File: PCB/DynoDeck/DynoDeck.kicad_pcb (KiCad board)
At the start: 2 copper layers, 0 parts

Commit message: Footprints
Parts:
- added BT1: Batt, Connector_JST:JST_PH_S2B-PH-K_1x02_P2.00mm_Horizontal, F.Cu at (137.2, 79.6)
- added C1: 47u, Capacitor_SMD:C_0603_1608Metric, F.Cu at (94.8, 78.4)
- added C10: 4u7, Capacitor_SMD:C_0603_1608Metric, F.Cu at (98.9, 78.4)
- added C11: 10u, Capacitor_SMD:C_0603_1608Metric, F.Cu at (98.9, 80.9)
- added C12: 10u, Capacitor_SMD:C_0603_1608Metric, F.Cu at (98.9, 83.5)
- added C13: 10u, Capacitor_SMD:C_0603_1608Metric, F.Cu at (98.9, 86.0)
- added C14: 4u7, Capacitor_SMD:C_0603_1608Metric, F.Cu at (98.9, 88.5)
- added C15: 47p, Capacitor_SMD:C_0603_1608Metric, F.Cu at (98.9, 91.0)
- added C16: 100n, Capacitor_SMD:C_0603_1608Metric, F.Cu at (98.9, 93.5)
- added C17: 47n, Capacitor_SMD:C_0603_1608Metric, F.Cu at (98.9, 96.0)
- added C18: 470n, Capacitor_SMD:C_0603_1608Metric, F.Cu at (98.9, 98.5)
- added C19: 4u7, Capacitor_SMD:C_0603_1608Metric, F.Cu at (102.9, 78.4)
- added C2: 100n, Capacitor_SMD:C_0603_1608Metric, F.Cu at (94.8, 80.9)
- added C20: 4u7, Capacitor_SMD:C_0603_1608Metric, F.Cu at (102.9, 80.9)
- added C21: 220n, Capacitor_SMD:C_0603_1608Metric, F.Cu at (102.9, 83.5)
- added C22: 100n, Capacitor_SMD:C_0603_1608Metric, F.Cu at (102.9, 86.0)
- added C24: 100n, Capacitor_SMD:C_0603_1608Metric, F.Cu at (102.9, 88.5)
- added C25: 100p, Capacitor_SMD:C_0402_1005Metric, F.Cu at (143.2, 96.0)
- added C26: 100n, Capacitor_SMD:C_0603_1608Metric, F.Cu at (102.9, 91.0)
- added C27: 10u, Capacitor_SMD:C_0603_1608Metric, F.Cu at (102.9, 93.5)
- added C3: 1u, Capacitor_SMD:C_0603_1608Metric, F.Cu at (94.8, 83.5)
- added C4: 1u, Capacitor_SMD:C_0603_1608Metric, F.Cu at (94.8, 86.0)
- added C5: 10p, Capacitor_SMD:C_0603_1608Metric, F.Cu at (94.8, 88.5)
- added C6: 100n, Capacitor_SMD:C_0603_1608Metric, F.Cu at (94.8, 91.0)
- added C7: 100n, Capacitor_SMD:C_0603_1608Metric, F.Cu at (94.8, 93.5)
- added C8: 100n, Capacitor_SMD:C_0603_1608Metric, F.Cu at (94.8, 96.0)
- added C9: 47n, Capacitor_SMD:C_0603_1608Metric, F.Cu at (94.8, 98.5)
- added D1: STAT, LED_SMD:LED_0603_1608Metric, F.Cu at (103.3, 104.7)
- added D2: D_Schottky, Diode_SMD:D_SMB, F.Cu at (129.1, 97.2)
- added FB1: 600@100Mhz, Inductor_SMD:L_0603_1608Metric_Pad1.05x0.95mm_HandSolder, F.Cu at (95.0, 104.7)
- added FL1: 0900FM15K0039, RF_Converter:Balun_Johanson_0900FM15K0039, F.Cu at (143.5, 92.8)
- added J1: USB_C_Receptacle_USB2.0_16P, Connector_USB:USB_C_Receptacle_G-Switch_GT-USB-7010ASV, F.Cu at (118.7, 92.2)
- added J2: PGRM, PGRMPins:PogoPin_1x05_P2.54mm_Pad1.8mm, F.Cu at (94.7, 101.6)
- added J3: CardKB, Connector_JST:JST_PH_S4B-PH-K_1x04_P2.00mm_Horizontal, F.Cu at (115.9, 79.6)
- added J4: E-paper, Connector_PinSocket_2.54mm:PinSocket_2x04_P2.54mm_Vertical, F.Cu at (137.7, 58.9)
- added J5: HC-IPEX0125-01 (u.FL), Connector_Coaxial:U.FL_Molex_MCRF_73412-0110_Vertical, F.Cu at (109.7, 102.9)
- added J6: BWSMA-KWE-Z001 (SMA), Connector_Coaxial:SMA_BAT_Wireless_BWSMA-KWE-Z001, F.Cu at (129.5, 89.7)
- added L1: 2u2, Inductor_SMD:L_Sunlord_MWSA0503S, F.Cu at (138.0, 90.2)
- added L2: 47n, Inductor_SMD:L_1008_2520Metric, F.Cu at (144.6, 83.7)
- added L3: 15u, Inductor_SMD:L_Sunlord_MWSA0503S, F.Cu at (138.0, 97.0)
- added R1: 10k, Resistor_SMD:R_0603_1608Metric, F.Cu at (102.9, 96.0)
- added R10: 10k, Resistor_SMD:R_0603_1608Metric, F.Cu at (106.9, 96.0)
- added R11: 5k1, Resistor_SMD:R_0603_1608Metric, F.Cu at (106.9, 98.5)
- added R12: 100k, Resistor_SMD:R_0603_1608Metric, F.Cu at (110.9, 78.4)
- added R13: 100k, Resistor_SMD:R_0603_1608Metric, F.Cu at (110.9, 80.9)
- added R14: 100k, Resistor_SMD:R_0603_1608Metric, F.Cu at (110.9, 83.5)
- added R15: 887k, Resistor_SMD:R_0603_1608Metric, F.Cu at (110.9, 86.0)
- added R16: 10k, Resistor_SMD:R_0603_1608Metric, F.Cu at (110.9, 88.5)
- added R17: 47, Resistor_SMD:R_0603_1608Metric, F.Cu at (110.9, 91.0)
- added R18: 10k, Resistor_SMD:R_0603_1608Metric, F.Cu at (110.9, 93.5)
- added R19: 100k, Resistor_SMD:R_0603_1608Metric, F.Cu at (110.9, 96.0)
- added R2: 4k7, Resistor_SMD:R_0603_1608Metric, F.Cu at (102.9, 98.5)
- added R3: 10k, Resistor_SMD:R_0603_1608Metric, F.Cu at (106.9, 78.4)
- added R4: 4k7, Resistor_SMD:R_0603_1608Metric, F.Cu at (106.9, 80.9)
- added R5: 220, Resistor_SMD:R_0603_1608Metric, F.Cu at (106.9, 83.5)
- added R6: 10k, Resistor_SMD:R_0603_1608Metric, F.Cu at (106.9, 86.0)
- added R7: 260, Resistor_SMD:R_0603_1608Metric, F.Cu at (106.9, 88.5)
- added R8: 10k, Resistor_SMD:R_0603_1608Metric, F.Cu at (106.9, 91.0)
- added R9: 10k, Resistor_SMD:R_0603_1608Metric, F.Cu at (106.9, 93.5)
- added SW1: QON, Button_Switch_SMD:SW_SPST_TS-1088-xR020, F.Cu at (143.5, 58.9)
- added SW2: POWER, Button_Switch_SMD:SW_SPDT_CK_JS102011SAQN, F.Cu at (118.4, 101.9)
- added SW3: RESET, Button_Switch_SMD:SW_SPST_TS-1088-xR020, F.Cu at (143.5, 63.4)
- added SW4: IO1, Button_Switch_SMD:SW_SPST_PTS647_Sx38, F.Cu at (129.0, 103.2)
- added U1: BQ25895RTW, Package_DFN_QFN:Texas_RTW_WQFN-24-1EP_4x4mm_P0.5mm_EP2.7x2.7mm_ThermalVias, F.Cu at (143.1, 72.0)
- added U2: USBLC6-2SC6, Package_TO_SOT_SMD:SOT-23-6, F.Cu at (144.7, 79.6)
- added U3: SX1262IMLTRT, Package_DFN_QFN:QFN-24-1EP_4x4mm_P0.5mm_EP2.6x2.6mm, F.Cu at (137.7, 103.5)
- added U4: TUSB320, Package_DFN_QFN:Texas_X2QFN-12_1.6x1.6mm_P0.4mm, F.Cu at (143.7, 88.8)
- added U5: MD7218E33PC1, Package_TO_SOT_SMD:SOT-89-5, F.Cu at (136.2, 71.9)
- added U6: E73-2G4M08S1C, E73-2G4M08S1C:E73-2G4M08S1C, F.Cu at (112.8, 66.7)
- added U7: BGS12WN6E6327, Package_LGA:Infineon_PG-TSNP-6-10_0.7x1.1mm_0.7x1.1mm_P0.4mm, F.Cu at (141.5, 67.4)
- added U8: BGS12WN6E6327, Package_LGA:Infineon_PG-TSNP-6-10_0.7x1.1mm_0.7x1.1mm_P0.4mm, F.Cu at (144.1, 67.4)
- added Y1: OW7EL89CENUXK7YLC-32M, Oscillator:Oscillator_SMD_Abracon_ASDMB-4Pin_2.5x2.0mm, F.Cu at (99.2, 105.4)
- added Y3: 3N00032G33YC, Oscillator:Oscillator_SMD_Abracon_ASE-4Pin_3.2x2.5mm_HandSoldering, F.Cu at (144.0, 103.1)
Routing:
- net /DIn-: track 0.00 -> 2.40 mm
- net /DIn+: track 0.00 -> 2.40 mm
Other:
- copper layers 2 -> 4
- rule pad_to_mask_clearance: 0 -> 0.075

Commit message: Footprints
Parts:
- added J7: CardKBRef, CardKBRef:CardKBRef, F.Cu at (106.4, 71.7)
- J3: value CardKB -> CardKBConn
- J4: footprint Connector_PinSocket_2.54mm:PinSocket_2x04_P2.54mm_Vertical -> WeActStudio:weact_epaper_29
- moved J2 99.0 mm to (193.0, 112.5)
- moved C10 98.6 mm to (197.2, 72.2)
- moved C11 98.6 mm to (197.2, 74.7)
- moved C12 98.6 mm to (197.2, 77.2)
- moved C13 98.6 mm to (197.2, 79.7)
- moved C14 98.6 mm to (197.2, 82.2)
- moved C15 98.6 mm to (197.2, 84.7)
- moved C16 98.6 mm to (197.2, 87.2)
- moved C17 98.6 mm to (197.2, 89.8)
- moved C18 98.6 mm to (197.2, 92.3)
- moved C19 98.6 mm to (201.2, 72.2)
- moved C20 98.6 mm to (201.2, 74.7)
- moved C21 98.6 mm to (201.2, 77.2)
- moved C22 98.6 mm to (201.2, 79.7)
- moved C24 98.6 mm to (201.2, 82.2)
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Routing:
- net /DIn-: track 2.40 -> 0.00 mm
- net /DIn+: track 2.40 -> 0.00 mm

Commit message: rough layout
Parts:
- added H1: MountBTML, MountingHole:MountingHole_2.7mm_M2.5, F.Cu at (35.0, 131.0)
- added H2: MountBTMR, MountingHole:MountingHole_2.7mm_M2.5, F.Cu at (130.0, 131.0)
- BT1, C1, C10, C11, C12, C13, C14, C15, C16, C17, C18, C19, C2, C20, C21, C22, C24, C25, C26, C27, C3, C4, C5, C6, C7, C8, C9, D1, D2, FB1, FL1, J1, J2, J3, J5, J6, L1, L2, L3, R1, R10, R11, R12, R13, R14, R15, R16, R17, R18, R19, R2, R3, R4, R5, R6, R7, R8, R9, SW1, SW2, SW3, SW4, U1, U2, U3, U4, U5, U6, Y1, Y3: moved to B.Cu
- U7, U8: value BGS12WN6E6327 -> PE42422MLAA-Z; footprint Package_LGA:Infineon_PG-TSNP-6-10_0.7x1.1mm_0.7x1.1mm_P0.4mm -> PE42422:PE42422-QFN-12_L2.0-W2.0-P0.50-BL-EP; moved to B.Cu
- moved J2 180.2 mm to (23.0, 53.0), turned to -90 degrees
- moved Y3 154.4 mm to (56.0, 45.6), turned to -90 degrees
- moved U2 144.1 mm to (43.0, 103.0)
- moved J3 134.3 mm to (60.0, 122.5), turned to 180 degrees
- moved U6 128.4 mm to (43.5, 37.8), turned to 180 degrees
- moved C25 126.5 mm to (115.0, 37.0), turned to 90 degrees
- moved J5 126.0 mm to (103.0, 32.5), turned to 180 degrees
- moved U8 122.0 mm to (115.0, 34.0), turned to -90 degrees
- moved J1 121.7 mm to (33.0, 103.5), turned to 90 degrees
- moved SW2 121.1 mm to (32.2, 118.0), turned to 90 degrees
- moved U7 115.7 mm to (115.0, 39.8), turned to 90 degrees
- moved U1 114.3 mm to (65.8, 103.7), turned to 180 degrees
- moved FL1 112.5 mm to (115.0, 43.1), turned to 90 degrees
- moved FB1 112.0 mm to (151.5, 37.7), turned to 180 degrees
- moved U3 108.2 mm to (114.0, 48.0), turned to 180 degrees
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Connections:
- net /SW_ANT renamed /SW_RFIO
- R17 pad 2: Net-(U7-CTRL) -> Net-(U7-V1)
- U7 pad 1: /SW_RFO -> GND
- U7 pad 2: GND -> /SW_RFI
- U7 pad 3: /SW_RFI -> GND
- U7 pad 4: +3V3 -> GND
- U7 pad 6: Net-(U7-CTRL) -> GND
- U8 pad 1: /ANT2 -> GND
- U8 pad 2: GND -> /ANT2
- U8 pad 3: /ANT1 -> GND
- U8 pad 4: +3V3 -> GND
- U8 pad 6: /ANT_CTRL -> GND
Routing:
- net /DIn+: track 0.00 -> 2.76 mm
- net /DIn-: track 0.00 -> 2.76 mm
- net +3V3: track 0.00 -> 1.68 mm, vias 0 -> 1
- added copper zone on In2.Cu, net +3V3
- added copper zone on In1.Cu, net GND
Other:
- board outline added: 105 x 107.3 mm

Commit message: Power Circuit
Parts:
- moved C16 154.0 mm to (42.0, 116.0), turned to -90 degrees
- moved C8 154.0 mm to (44.5, 106.4), turned to -90 degrees
- moved C1 142.8 mm to (58.8, 107.4), turned to 0 degrees
- moved R14 142.1 mm to (44.2, 116.0), turned to 90 degrees
- moved R15 142.0 mm to (42.3, 109.3)
- moved R12 139.4 mm to (47.0, 110.8)
- moved R13 139.4 mm to (47.0, 113.2)
- moved C19 139.3 mm to (58.1, 120.5)
- moved C14 135.2 mm to (62.0, 115.0), turned to -90 degrees
- moved C10 135.0 mm to (62.0, 104.0), turned to -90 degrees
- moved D2 134.9 mm to (53.0, 104.7), turned to 90 degrees
- moved C3 134.8 mm to (64.5, 99.8), turned to 90 degrees
- moved C9 133.7 mm to (64.5, 104.0), turned to 90 degrees
- moved C27 133.5 mm to (57.0, 102.5), turned to -90 degrees
- moved U5 130.9 mm to (57.0, 115.8), turned to 0 degrees
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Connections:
- U4 pad 1: /CC1 -> /CC2
- U4 pad 2: /CC2 -> /CC1
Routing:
- net /D-: track 0.00 -> 102.7 mm
- net /D+: track 0.00 -> 100.9 mm, vias 0 -> 2
- net VBUS: track 0.00 -> 70.8 mm, vias 0 -> 9
- net /SYS: track 0.00 -> 45.9 mm, vias 0 -> 2
- net /EN: track 0.00 -> 26.0 mm
- net Net-(U1-TS): track 0.00 -> 22.1 mm, vias 0 -> 2
- net /CC2: track 0.00 -> 20.1 mm
- net /CC1: track 0.00 -> 15.7 mm
- net /PMID: track 0.00 -> 14.5 mm
- net Net-(C9-Pad1): track 0.00 -> 10.1 mm
- net Net-(U1-REGN): track 0.00 -> 7.89 mm
- net /~{CE}: track 0.00 -> 6.93 mm
- net Net-(U1-ILIM): track 0.00 -> 5.65 mm
- net /OTG: track 0.00 -> 5.46 mm
- net /DIn-: track 2.76 -> 8.21 mm
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- added copper zone on B.Cu, net +3V3
- added copper zone on B.Cu, net /BATT+
- added copper zone on B.Cu, net /SYS
- added copper zone on B.Cu, net GND
- added copper zone on B.Cu, net VBUS
- added copper zone on F.Cu, net VBUS

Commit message: Part of Sx1262
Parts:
- C24, C26: footprint Capacitor_SMD:C_0603_1608Metric -> Capacitor_SMD:C_0402_1005Metric
- FB1: footprint Inductor_SMD:L_0603_1608Metric_Pad1.05x0.95mm_HandSolder -> Inductor_SMD:L_0603_1608Metric
- L2: footprint Inductor_SMD:L_1008_2520Metric -> Inductor_SMD:L_0402_1005Metric
- moved C24 92.6 mm to (115.8, 30.2), turned to 0 degrees
- moved C6 92.1 mm to (113.1, 52.4)
- moved C17 90.3 mm to (119.0, 42.8), turned to 0 degrees
- moved C26 89.6 mm to (114.1, 40.4)
- moved C7 89.6 mm to (120.0, 46.5), turned to 0 degrees
- moved C4 88.9 mm to (113.1, 56.6)
- moved C5 86.8 mm to (119.2, 49.0), turned to -90 degrees
- moved C15 86.6 mm to (119.0, 44.8), turned to 0 degrees
- moved R8 86.2 mm to (109.3, 48.7), turned to 0 degrees
- moved L3 85.1 mm to (119.8, 54.8), turned to 0 degrees
- moved C2 80.2 mm to (124.5, 46.0)
- moved R17 77.6 mm to (112.0, 54.5)
- moved R5 71.8 mm to (121.5, 49.0), turned to -90 degrees
- moved C18 65.1 mm to (151.0, 46.8)
- moved J2 48.8 mm to (66.3, 30.6), turned to 0 degrees
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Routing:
- net /D-: track 102.7 -> 46.6 mm
- net /D+: track 100.9 -> 44.8 mm
- net VBUS: track 70.8 -> 18.5 mm, vias 9 -> 8
- net /DIO3: track 0.00 -> 12.3 mm
- net Net-(U3-VREG): track 0.00 -> 9.98 mm
- net GND: track 3.81 -> 11.3 mm, vias 1 -> 11
- net Net-(U3-DCC_SW): track 0.00 -> 7.08 mm
- net Net-(U3-VR_PA): track 0.00 -> 6.10 mm
- net /SW_RFI: track 0.00 -> 5.62 mm
- net /~{SxRESET}: track 0.00 -> 4.82 mm
- net /SxBUSY: track 0.00 -> 4.40 mm
- net Net-(Y1-VDD): track 0.00 -> 4.37 mm
- net /DIO1: track 0.00 -> 4.36 mm
- net /SW_RFO: track 0.00 -> 4.32 mm
- net /DIO2: track 0.00 -> 4.30 mm
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
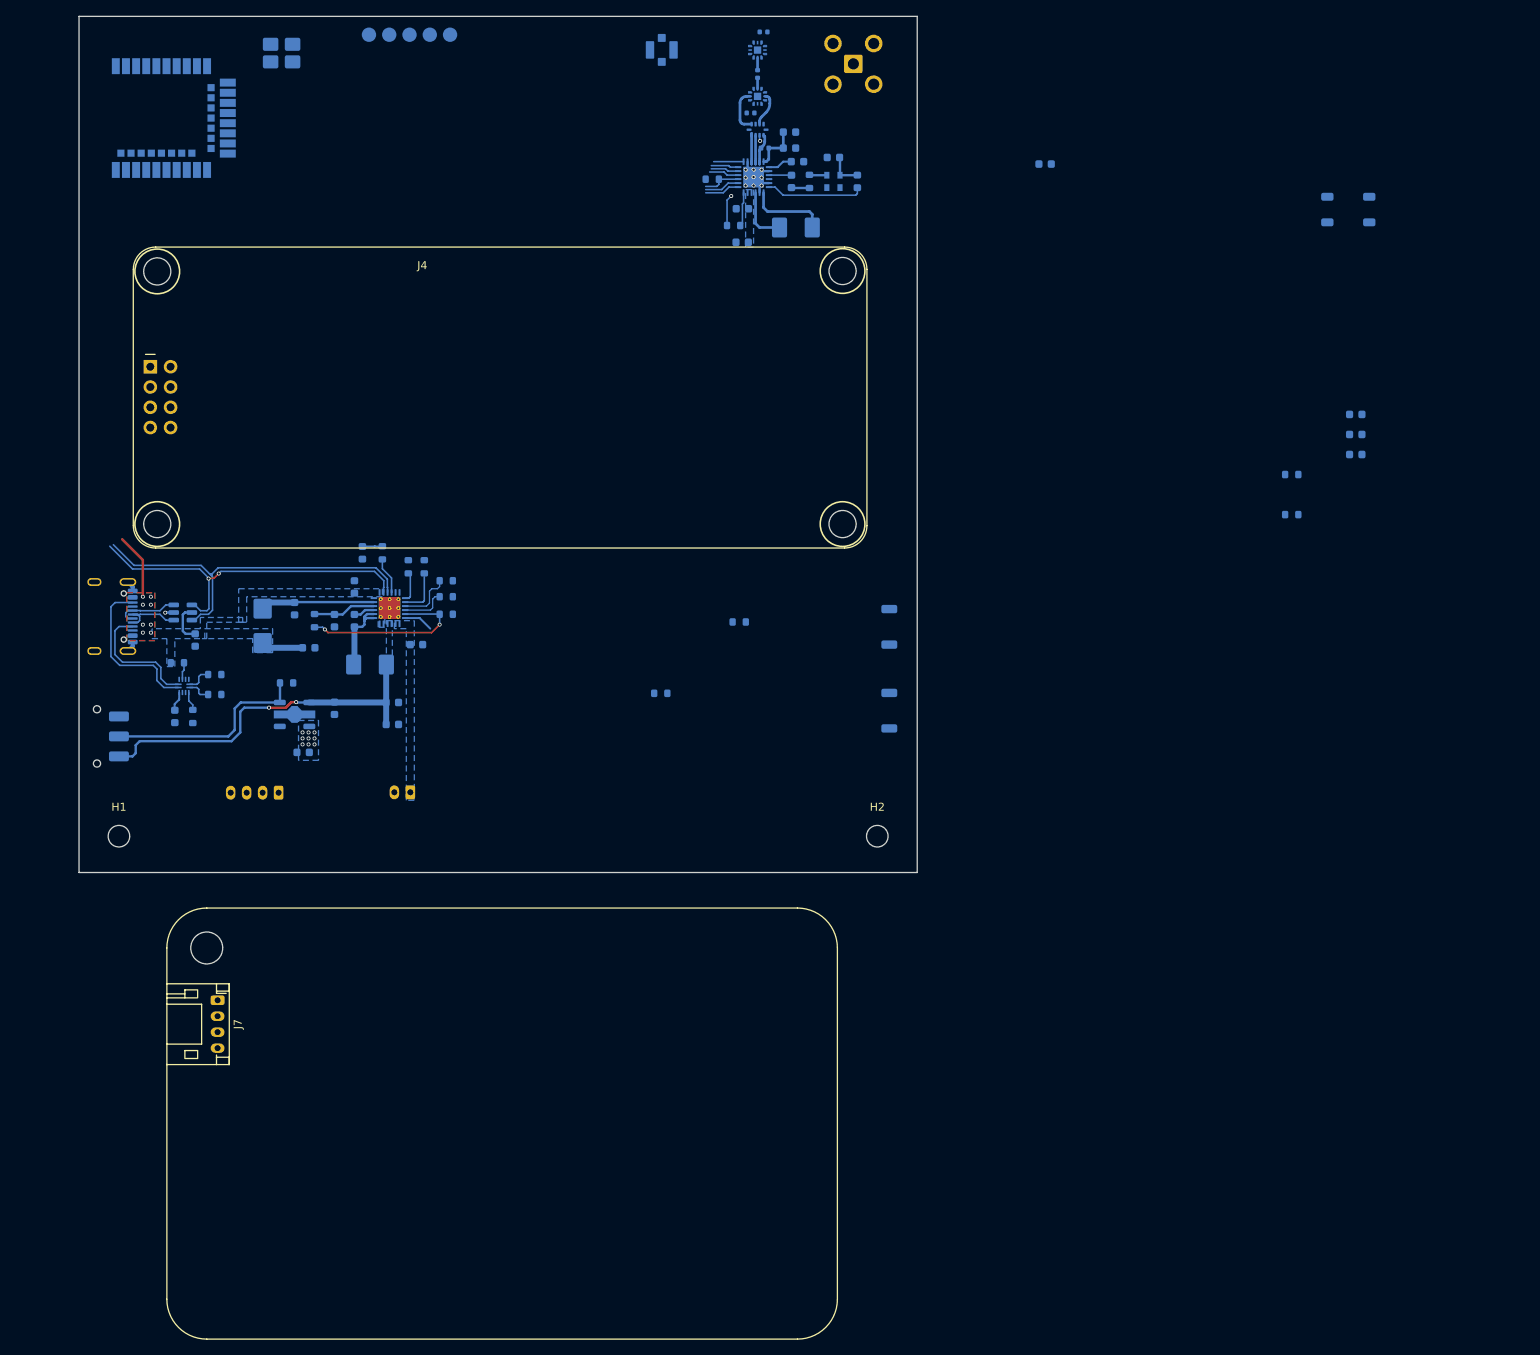
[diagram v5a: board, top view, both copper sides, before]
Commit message: nRF52840 remapping
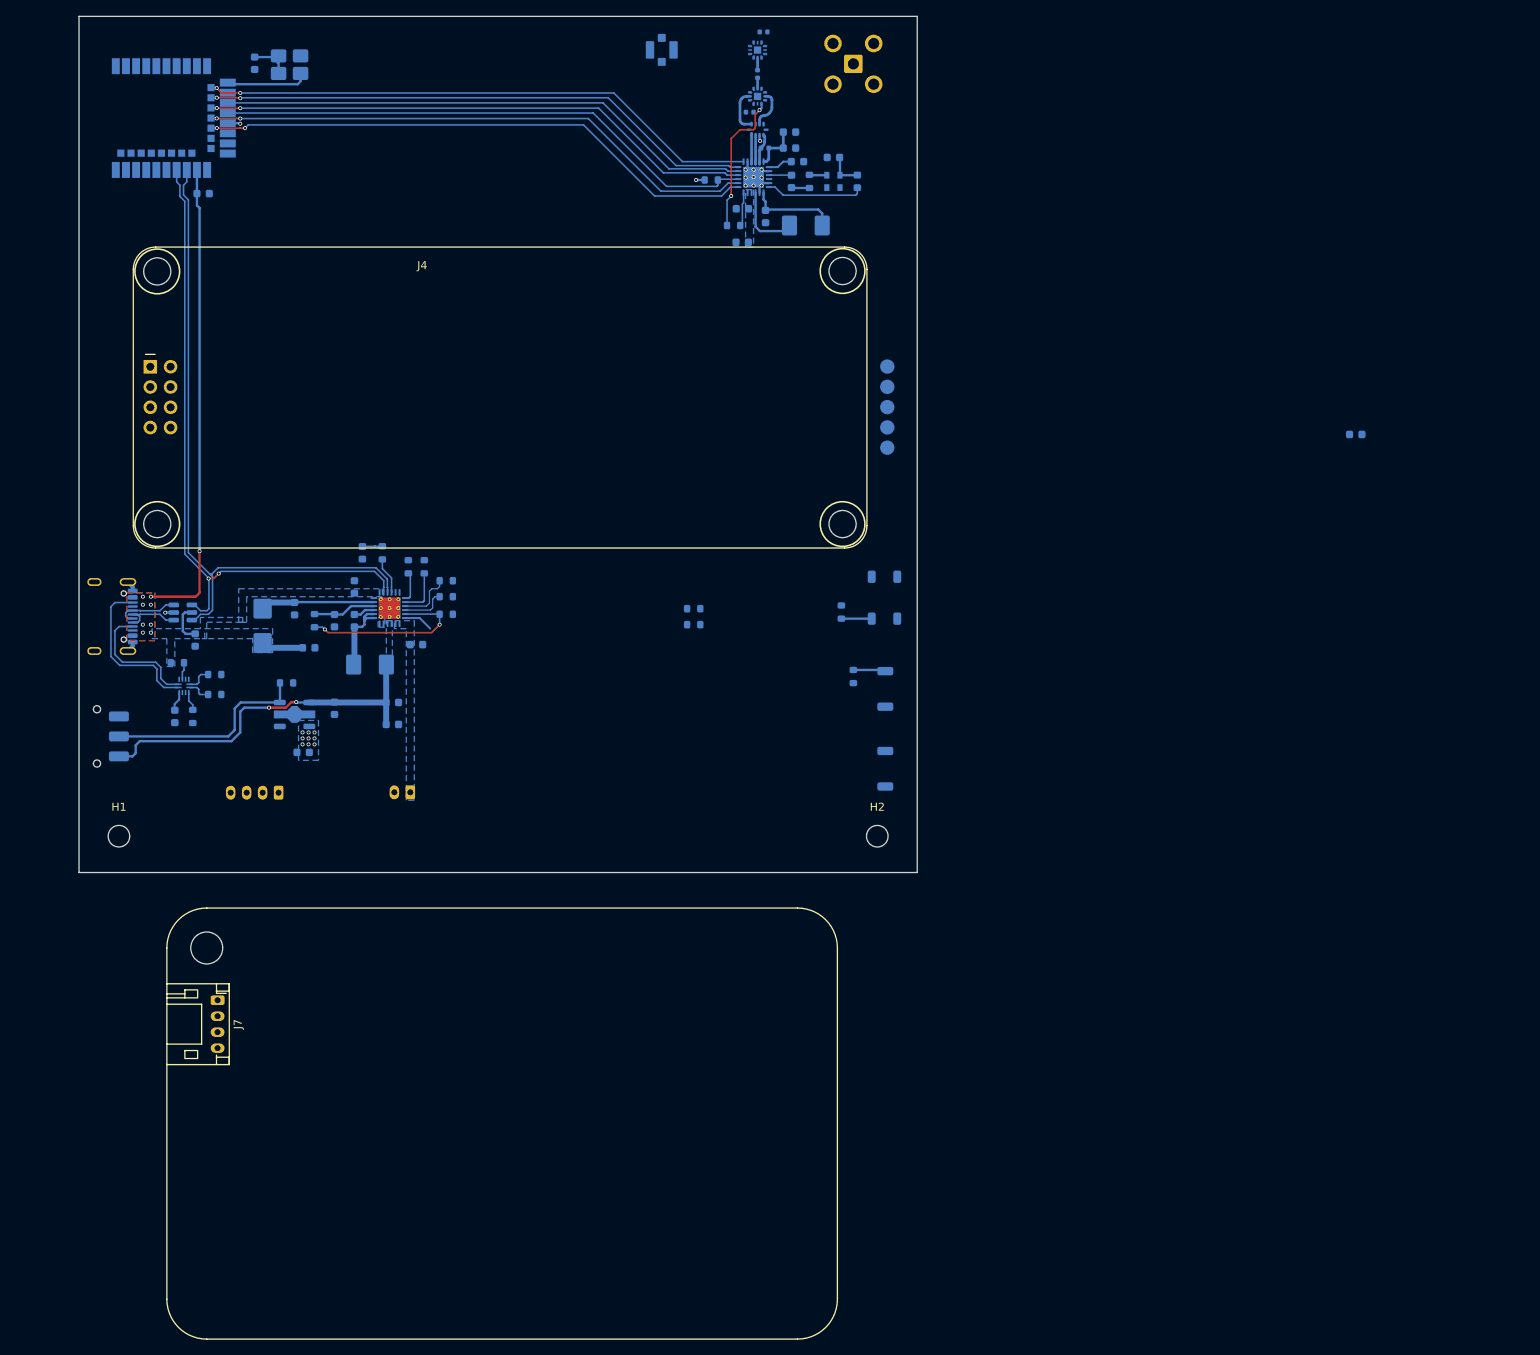
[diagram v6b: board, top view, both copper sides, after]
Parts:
- moved C20 147.0 mm to (45.5, 50.5), turned to 0 degrees
- moved C22 146.4 mm to (52.0, 34.2), turned to -90 degrees
- moved J2 77.1 mm to (131.2, 72.2), turned to -90 degrees
- moved SW4 75.8 mm to (130.9, 101.1), turned to -90 degrees
- moved R16 60.5 mm to (127.0, 111.0), turned to 90 degrees
- moved R18 57.7 mm to (125.5, 102.9), turned to -90 degrees
- moved C18 35.6 mm to (116.0, 53.4), turned to -90 degrees
- moved R2 9.54 mm to (107.0, 104.5)
- moved SW3 7.79 mm to (131.0, 112.5)
- moved SW1 7.29 mm to (131.0, 122.5), turned to -90 degrees
- moved R4 5.94 mm to (107.0, 102.5)
- moved Y3 1.76 mm to (56.4, 34.4)
- moved L3 1.27 mm to (121.0, 54.5)
- moved R8 0.16 mm to (109.2, 48.8)
- moved C26 0.14 mm to (114.0, 40.3)
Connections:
- U6 pad 12: unconnected-(U6B-P0.26-Pad12) -> /SxNSS
- U6 pad 14: /SCL -> /SCK
- U6 pad 15: /SDA -> /MOSI
- U6 pad 16: /DC -> /MISO
- U6 pad 17: /SxBUSY -> /~{SxRESET}
- U6 pad 18: /DIO1 -> /SxBUSY
- U6 pad 20: unconnected-(U6B-P0.12-Pad20) -> /DIO1
- U6 pad 22: /SxNSS -> unconnected-(U6B-P0.07-Pad22)
- U6 pad 30: /SCK -> unconnected-(U6B-P0.17-Pad30)
- U6 pad 32: /MOSI -> unconnected-(U6B-P0.20-Pad32)
- U6 pad 33: /MISO -> unconnected-(U6B-P0.13-Pad33)
- U6 pad 38: /~{SxRESET} -> unconnected-(U6C-P1.02-Pad38)
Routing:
- net /SxNSS: track 3.75 -> 70.5 mm, vias 0 -> 2
- net /SCK: track 3.44 -> 69.7 mm, vias 0 -> 2
- net /DIO1: track 4.36 -> 70.3 mm, vias 0 -> 2
- net /SxBUSY: track 4.40 -> 70.2 mm, vias 0 -> 2
- net /MISO: track 3.72 -> 69.5 mm, vias 0 -> 2
- net /MOSI: track 3.48 -> 67.5 mm
- net /~{SxRESET}: track 4.82 -> 68.3 mm
- net VBUS: track 18.5 -> 70.1 mm, vias 8 -> 9
- net /D+: track 44.8 -> 83.5 mm
- net /D-: track 46.6 -> 85.2 mm
- net Net-(U7-V1): track 3.92 -> 18.0 mm, vias 1 -> 2
- net /XL1: track 0.00 -> 10.2 mm
- net +3V3: track 5.49 -> 13.4 mm, vias 9 -> 11
- net /nRESET: track 0.00 -> 4.06 mm
- net /USER1: track 0.00 -> 3.80 mm
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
